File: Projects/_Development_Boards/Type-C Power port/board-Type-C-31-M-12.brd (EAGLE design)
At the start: 12.5 x 19 mm, 2 parts, among them J1 TYPE-C-31-M-17

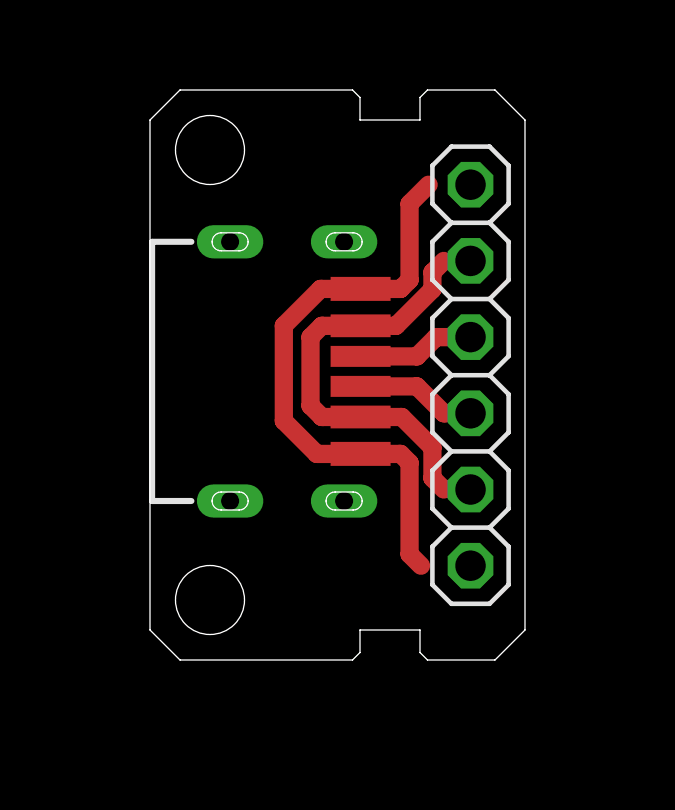
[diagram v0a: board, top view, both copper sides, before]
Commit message: Type-C power port PCB panelized
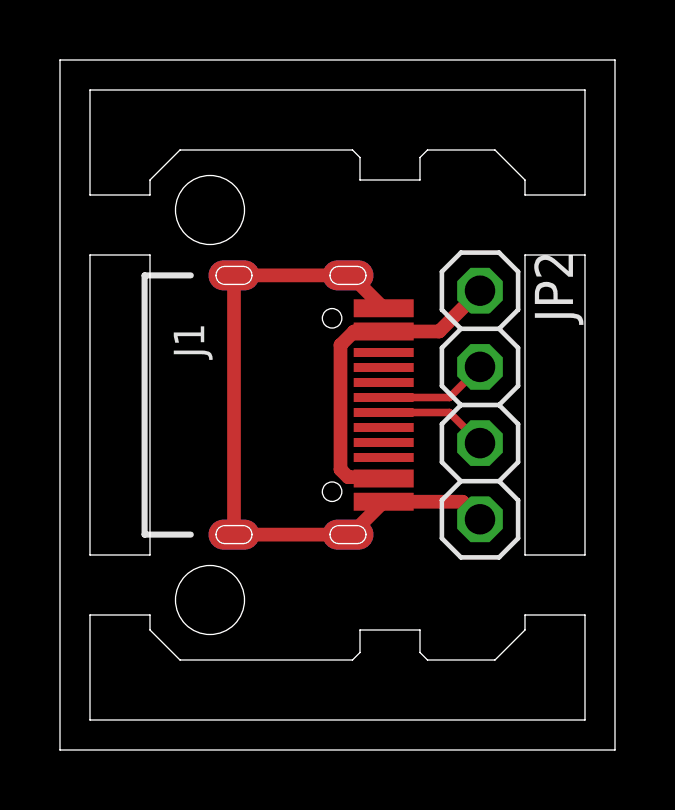
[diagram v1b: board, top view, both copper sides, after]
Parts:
- removed JP1: (no value), pinhead_v2:1X06/OCT
- added JP2: (no value), pinhead_v2:1X04/OCT
- J1: value TYPE-C-31-M-17 -> USB-TYPE-C-31-M-12; device angrypig7_Library:TYPE-C-31-M-17 -> angrypig7-Connectors:USB-TYPE-C-31-M-12
- moved J1 1.12 mm to (6.60, 8.50)
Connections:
- net N$1: now also J1.VBUS1, J1.VBUS2, JP2.1; no longer J1.VBUS, J1.VBUS_2, JP1.2, JP1.5
- net N$2: now also J1.A6, JP2.2; no longer J1.GND, J1.GND_2, JP1.1, JP1.6
- net N$3: now also J1.A7, JP2.3; no longer J1.CC1, JP1.4
- net N$4: now also J1.GND1, J1.GND2, J1.SHLD-B1, J1.SHLD-B2, J1.SHLD-B3, J1.SHLD-B4, J1.SHLD-T1, J1.SHLD-T2, J1.SHLD-T3, J1.SHLD-T4, JP2.4; no longer J1.CC2, JP1.3
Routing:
- net N$4: track 4.04 -> 23.0 mm
- net N$2: track 19.8 -> 3.63 mm
- net N$1: track 14.3 -> 11.1 mm
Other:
- board size 12.5 x 19 mm -> 18.5 x 23 mm
- board text added: "D+"
- board text added: "D-"
- board text removed: "CC1"
- board text removed: "CC2"
